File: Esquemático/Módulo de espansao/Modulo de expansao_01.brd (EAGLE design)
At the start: 86.3 x 84.8 mm, 92 parts, among them IC1 MCP25050-I/P, IC2 MCP2551-I/P, IC3 LM1117T-3.3/NOPB, K1 AQV21, K2 AQV21, K3 AQV21, K4 AQV21, K5 AQV21, K6 AQV21, Q2 20M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

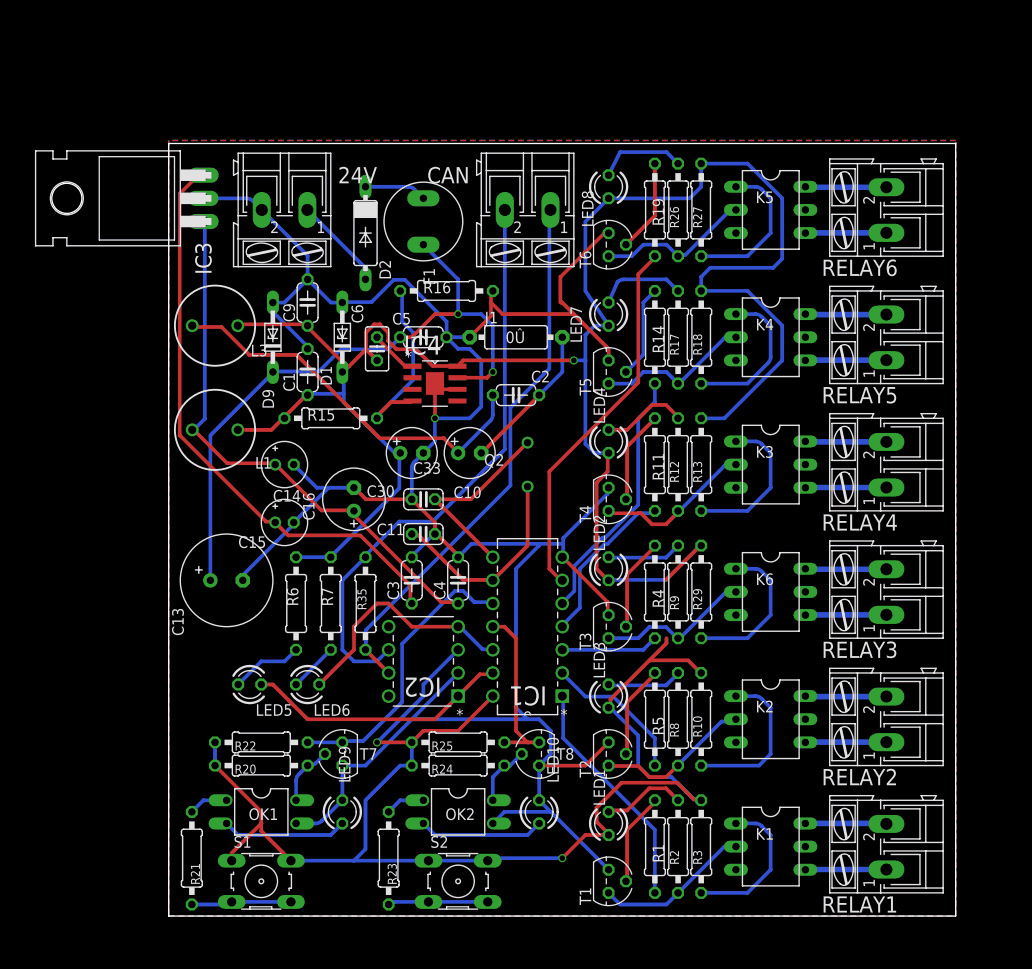
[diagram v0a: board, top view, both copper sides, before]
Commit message: modulo de expansao final
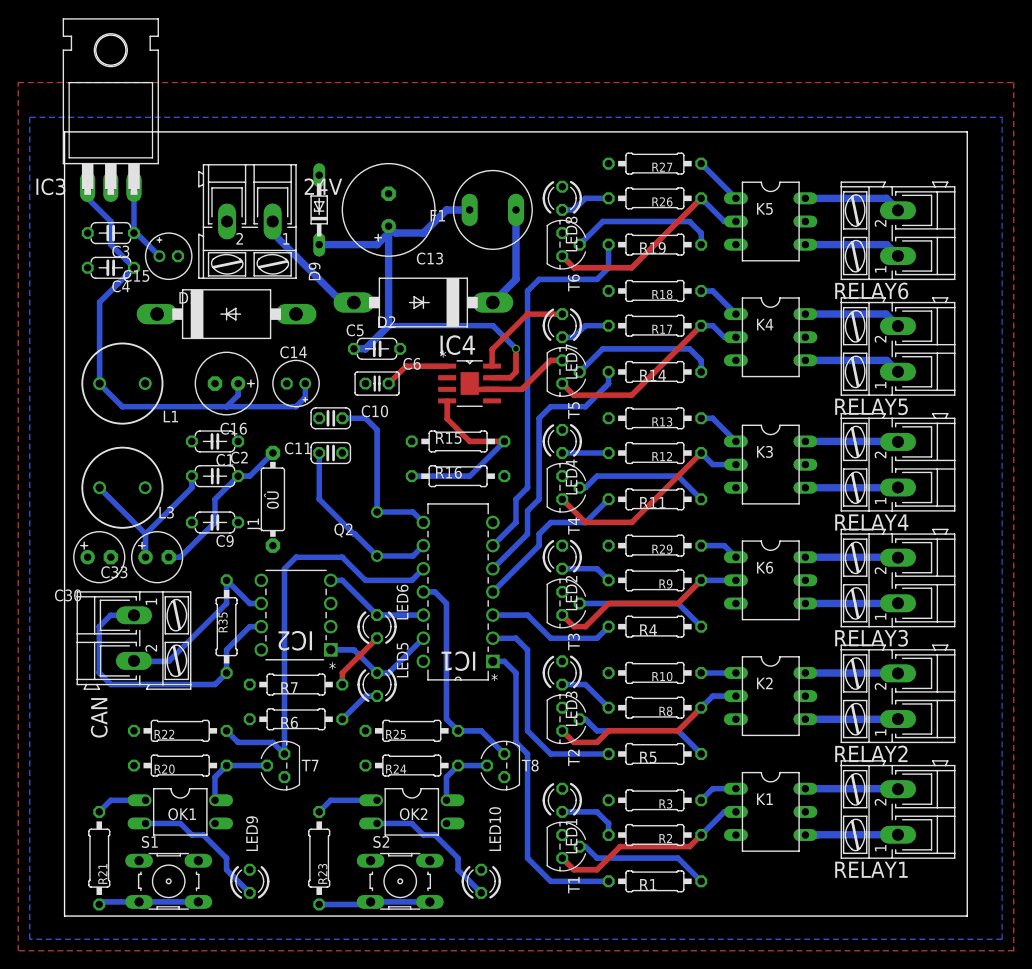
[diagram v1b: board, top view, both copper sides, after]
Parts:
- D1: device diode:DO34Z7 -> diode:C2673
- D2: device diode:DO07 -> diode:C2673
- moved CAN 63.8 mm to (-3.81, 30.5), turned to 270 degrees
- moved C4 51.3 mm to (-6.35, 71.1), turned to 180 degrees
- moved C3 50.4 mm to (-6.35, 74.9), turned to 180 degrees
- moved C13 44.4 mm to (24.1, 77.5), turned to 90 degrees
- moved C33 36.1 mm to (-1.27, 39.4)
- moved C30 36.1 mm to (-7.62, 39.4)
- moved C2 34.2 mm to (5.08, 48.3)
- moved J1 32.1 mm to (11.4, 45.7), turned to 90 degrees
- moved C15 31.9 mm to (0.00, 72.4)
- moved C9 26.2 mm to (5.08, 43.2), turned to 180 degrees
- moved L3 20.5 mm to (-5.08, 47.0)
- moved R16 20.4 mm to (31.8, 48.3)
- moved C16 18.9 mm to (6.35, 58.4), turned to 180 degrees
- moved Q2 18.2 mm to (22.9, 41.9)
- moved R35 15.5 mm to (6.35, 31.8)
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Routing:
- net 5V: track 379.5 -> 11.1 mm, vias 3 -> 0
- net GND: track 287.4 -> 11.7 mm, vias 1 -> 0
- net +3.3V: track 64.1 -> 8.93 mm
- net N$31: track 63.9 -> 20.2 mm
- net N$32: track 60.3 -> 31.8 mm
- net VCC/2: track 42.8 -> 18.2 mm
- net TXCAN: track 29.1 -> 12.8 mm
- net N$21: track 71.4 -> 56.2 mm, vias 2 -> 1
- net RXCAN: track 26.3 -> 11.7 mm
- net N$43: track 17.5 -> 3.81 mm
- net GP6: track 31.5 -> 45.1 mm
- net N$45: track 16.8 -> 4.34 mm
- net N$48: track 16.8 -> 4.34 mm
- net N$46: track 16.8 -> 4.86 mm
- net N$44: track 16.7 -> 4.86 mm
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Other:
- board size 86.3 x 84.8 mm -> 99 x 86 mm
